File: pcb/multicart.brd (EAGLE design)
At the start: 58.1 x 85.1 mm, 20 parts, among them IC1 27C64-27C080, IC2 74HCT373N, IC3 74HCT08N, Q1 BS170

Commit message: Adjusted the PCB dimension for manufacture.
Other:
- board size 58.1 x 85.1 mm -> 63.5 x 88.3 mm

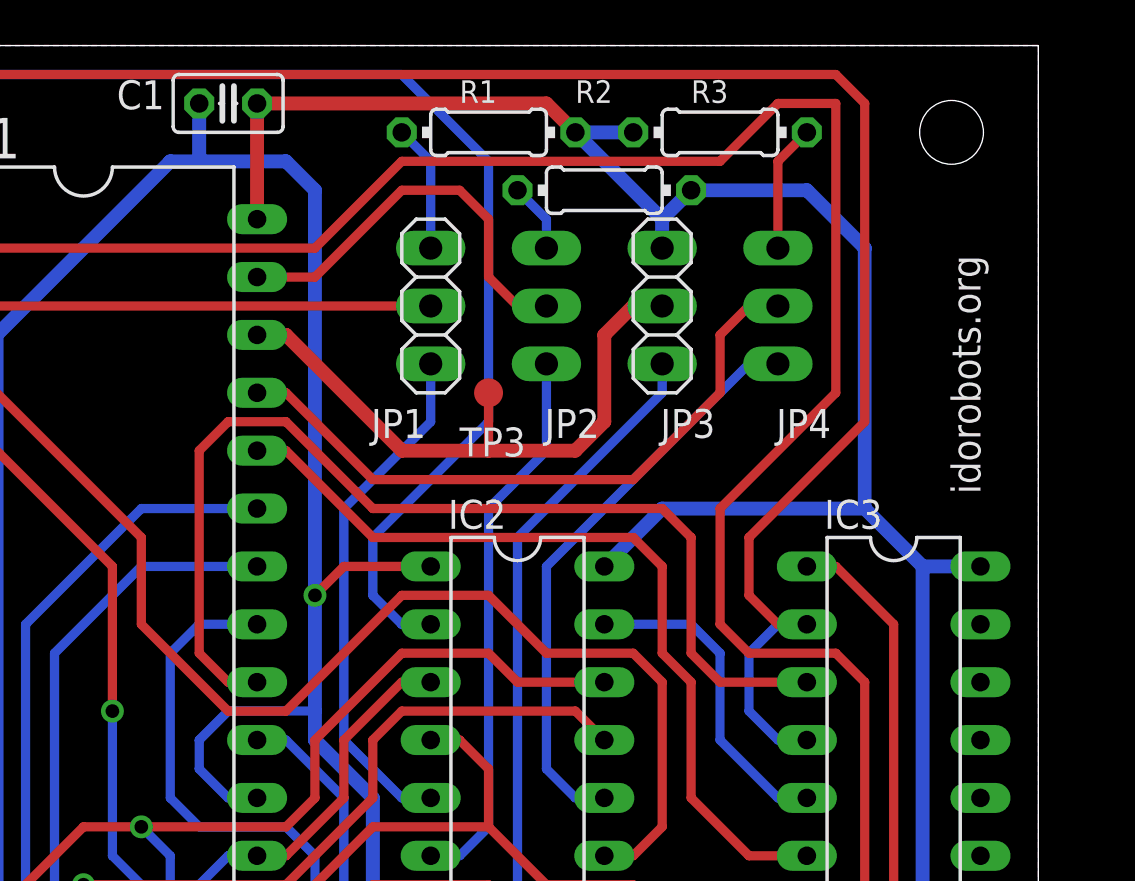
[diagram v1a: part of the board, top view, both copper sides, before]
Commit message: Adjusted some traces for manufacture.
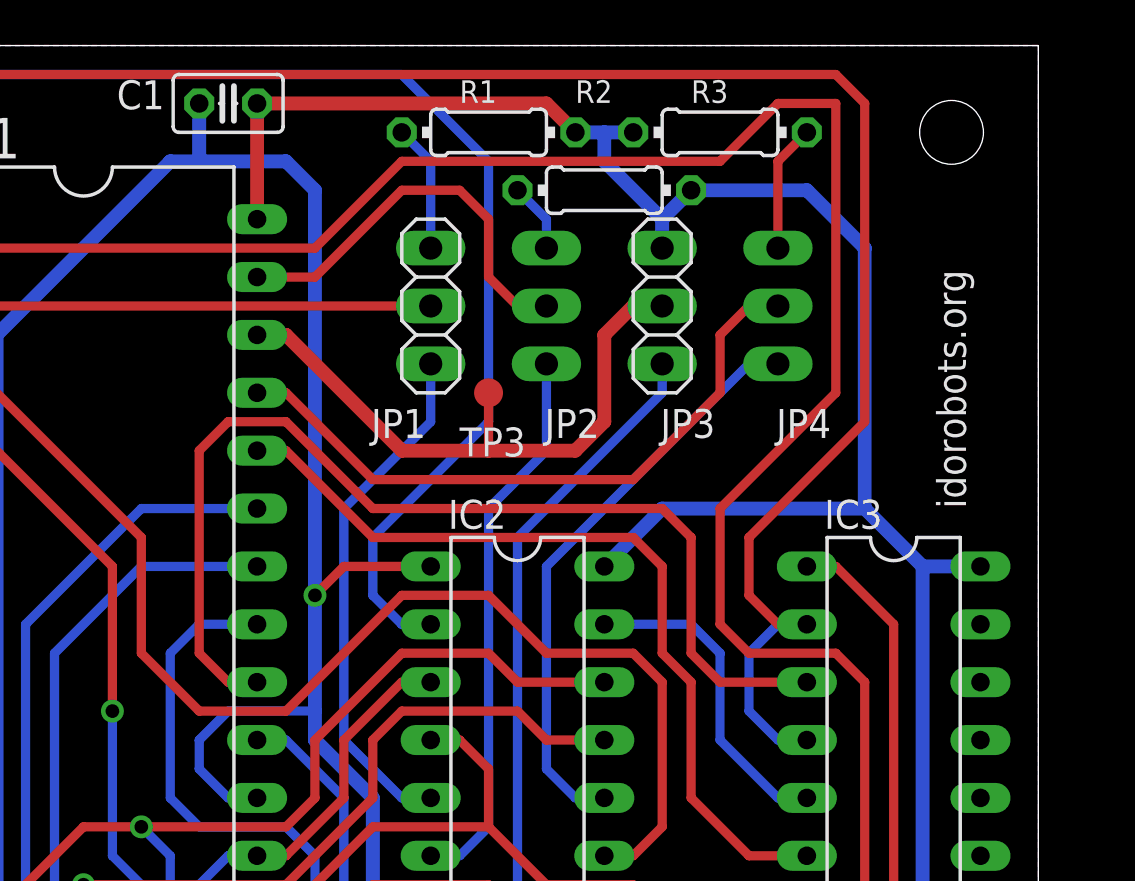
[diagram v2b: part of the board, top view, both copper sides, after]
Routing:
- net N$3: track 55.2 -> 55.9 mm
- net VCC: track 171.2 -> 170.7 mm
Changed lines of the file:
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@@
 <layer number="17" name="Pads" color="2" fill="1" visible="yes" active="yes"/>
 <layer number="18" name="Vias" color="2" fill="1" visible="yes" active="yes"/>
-<layer number="19" name="Unrouted" color="6" fill="1" visible="no" active="yes"/>
+<layer number="19" name="Unrouted" color="6" fill="1" visible="yes" active="yes"/>
 <layer number="20" name="Dimension" color="15" fill="1" visible="yes" active="yes"/>
 <layer number="21" name="tPlace" color="7" fill="1" visible="yes" active="yes"/>
 <layer number="22" name="bPlace" color="7" fill="1" visible="yes" active="yes"/>
-<layer number="23" name="tOrigins" color="15" fill="1" visible="no" active="yes"/>
+<layer number="23" name="tOrigins" color="15" fill="1" visible="yes" active="yes"/>
 <layer number="24" name="bOrigins" color="15" fill="1" visible="no" active="yes"/>
 <layer number="25" name="tNames" color="7" fill="1" visible="yes" active="yes"/>
@@
 <text x="24.765" y="15.24" size="2.54" layer="21" font="vector" rot="R180" align="center">Atari XE</text>
 <text x="44.45" y="15.24" size="2.54" layer="21" font="vector" rot="R180" align="center">Multicart</text>
-<text x="60.96" y="62.865" size="1.27" layer="21" font="vector" rot="R90">idorobots.org</text>
+<text x="60.325" y="62.23" size="1.27" layer="21" font="vector" rot="R90">idorobots.org</text>
 <text x="34.29" y="11.43" size="1.27" layer="21" font="vector" rot="R180" align="center">rev. 2.0</text>
 <hole x="8.89" y="78.74" drill="2.8"/>
@@
 <wire x1="39.37" y1="58.42" x2="35.56" y2="58.42" width="0.4064" layer="1"/>
 <wire x1="35.56" y1="58.42" x2="30.48" y2="53.34" width="0.4064" layer="1"/>
-<wire x1="30.48" y1="53.34" x2="27.94" y2="53.34" width="0.4064" layer="1"/>
-<wire x1="27.94" y1="53.34" x2="24.13" y2="57.15" width="0.4064" layer="1"/>
-<wire x1="24.13" y1="57.15" x2="24.13" y2="60.96" width="0.4064" layer="1"/>
+<wire x1="30.48" y1="53.34" x2="26.67" y2="53.34" width="0.4064" layer="1"/>
+<wire x1="24.13" y1="55.88" x2="24.13" y2="60.96" width="0.4064" layer="1"/>
 <wire x1="24.13" y1="60.96" x2="15.24" y2="69.85" width="0.4064" layer="1"/>
 <contactref element="IC1" pad="3"/>
 <wire x1="13.97" y1="69.85" x2="15.24" y2="69.85" width="0.4064" layer="1"/>
+<wire x1="26.67" y1="53.34" x2="24.13" y2="55.88" width="0.4064" layer="1"/>
 </signal>
 <signal name="N$4">
@@
 <via x="21.59" y="45.72" extent="1-16" drill="0.6" shape="octagon"/>
 <wire x1="35.56" y1="25.4" x2="22.86" y2="38.1" width="0.4064" layer="16"/>
-<wire x1="35.56" y1="53.34" x2="43.18" y2="53.34" width="0.4064" layer="1"/>
-<wire x1="43.18" y1="53.34" x2="44.45" y2="52.07" width="0.4064" layer="1"/>
 <wire x1="35.56" y1="20.32" x2="35.56" y2="25.4" width="0.4064" layer="16"/>
 <wire x1="22.86" y1="38.1" x2="22.86" y2="44.45" width="0.4064" layer="16"/>
@@
 <wire x1="34.29" y1="49.53" x2="34.29" y2="52.07" width="0.4064" layer="1"/>
 <wire x1="34.29" y1="52.07" x2="35.56" y2="53.34" width="0.4064" layer="1"/>
+<wire x1="35.56" y1="53.34" x2="40.64" y2="53.34" width="0.4064" layer="1"/>
+<wire x1="40.64" y1="53.34" x2="41.91" y2="52.07" width="0.4064" layer="1"/>
+<wire x1="41.91" y1="52.07" x2="44.45" y2="52.07" width="0.4064" layer="1"/>
 </signal>
 <signal name="D2">
@@
 <wire x1="48.26" y1="76.2" x2="46.99" y2="74.93" width="0.6096" layer="16"/>
 <wire x1="46.99" y1="73.66" x2="46.99" y2="74.93" width="0.6096" layer="16"/>
-<wire x1="46.99" y1="74.93" x2="43.18" y2="78.74" width="0.6096" layer="16"/>
-<wire x1="43.18" y1="78.74" x2="45.72" y2="78.74" width="0.6096" layer="16"/>
+<wire x1="43.18" y1="78.74" x2="44.45" y2="78.74" width="0.6096" layer="16"/>
+<wire x1="44.45" y1="78.74" x2="45.72" y2="78.74" width="0.6096" layer="16"/>
 <wire x1="29.21" y1="80.01" x2="41.91" y2="80.01" width="0.6096" layer="1"/>
 <wire x1="41.91" y1="80.01" x2="43.18" y2="78.74" width="0.6096" layer="1"/>
@@
 <contactref element="TP2" pad="TP"/>
 <wire x1="46.99" y1="31.75" x2="45.085" y2="29.845" width="0.4064" layer="1"/>
+<wire x1="46.99" y1="74.93" x2="44.45" y2="77.47" width="0.6096" layer="16"/>
+<wire x1="44.45" y1="77.47" x2="44.45" y2="78.74" width="0.6096" layer="16"/>
 </signal>
 <signal name="GND">
